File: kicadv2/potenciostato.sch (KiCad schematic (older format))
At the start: 33 parts, among them J10 test_GND, J11 test_GND, J12 test_GND, J13 AC2, J14 Conn_Coaxial, J3 Conn_01x03_Male, J4 test_I, J5 test_V, J6 test_VIN, J9 AC1, U1 OP77, U2 TL082, U3 OP77, U4 OP77, U5 4316, U6 L7805, U8 L7905

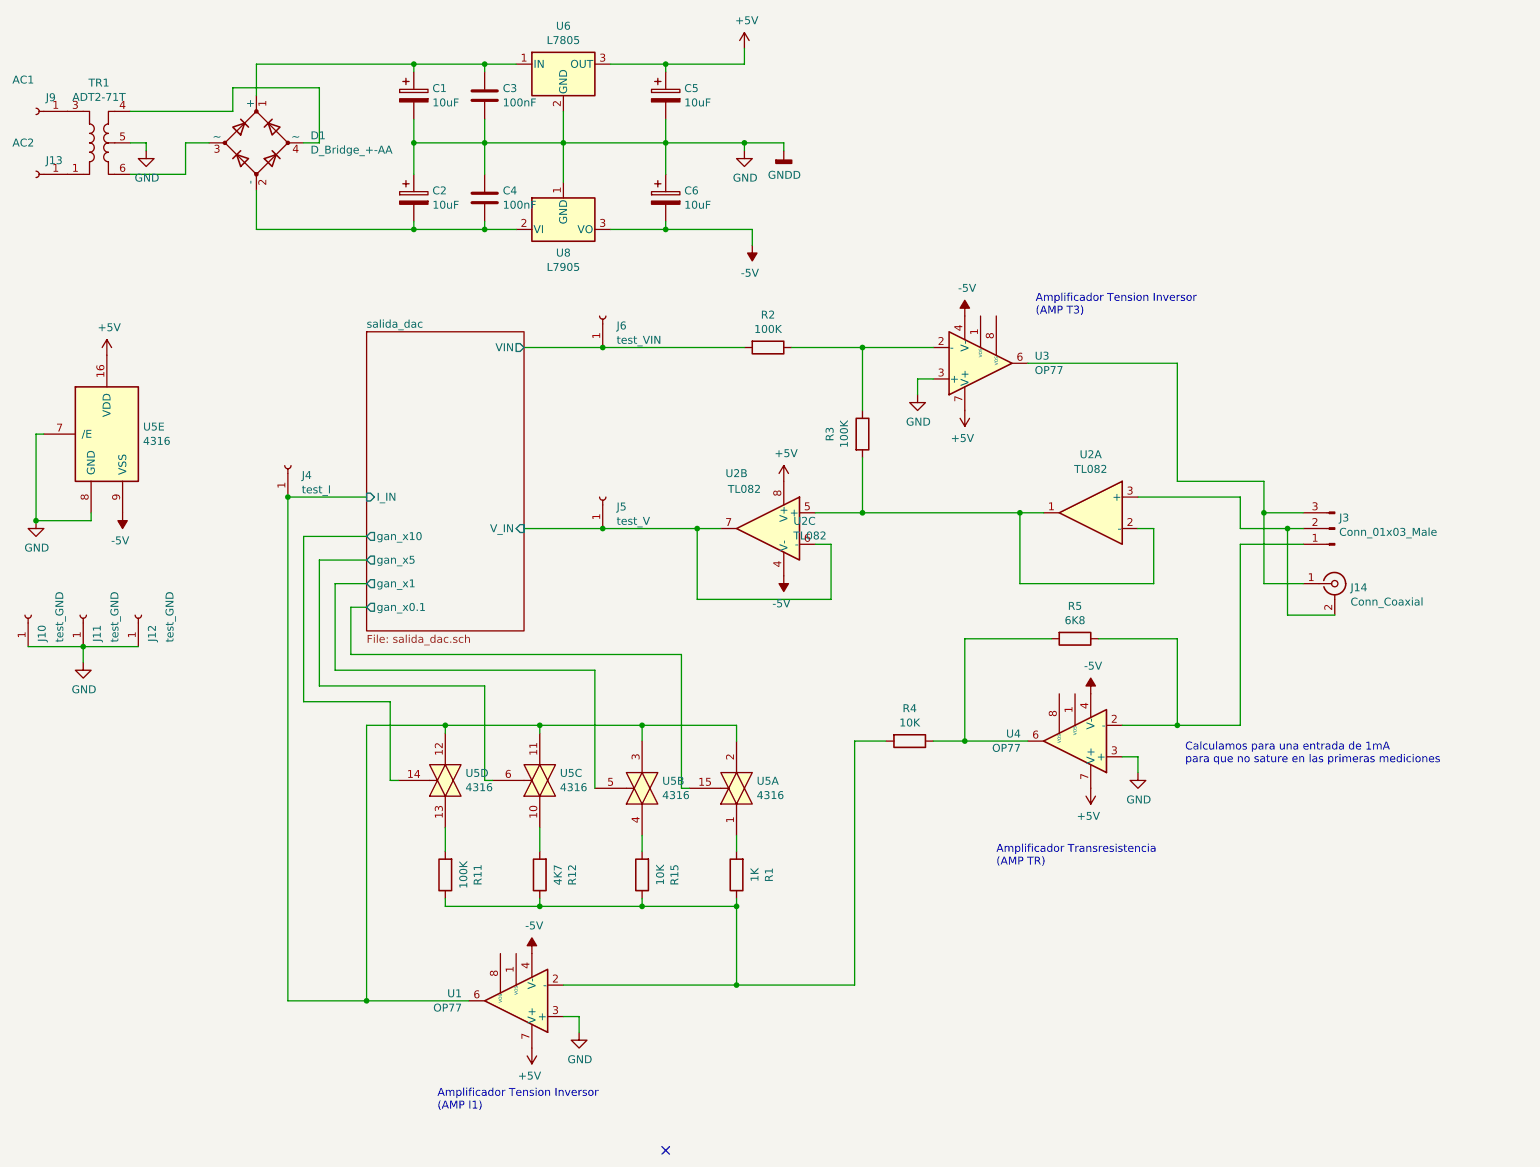
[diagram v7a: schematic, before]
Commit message: finalizado (casi) f silk, falta mover BNC para que no choqeu con LPC
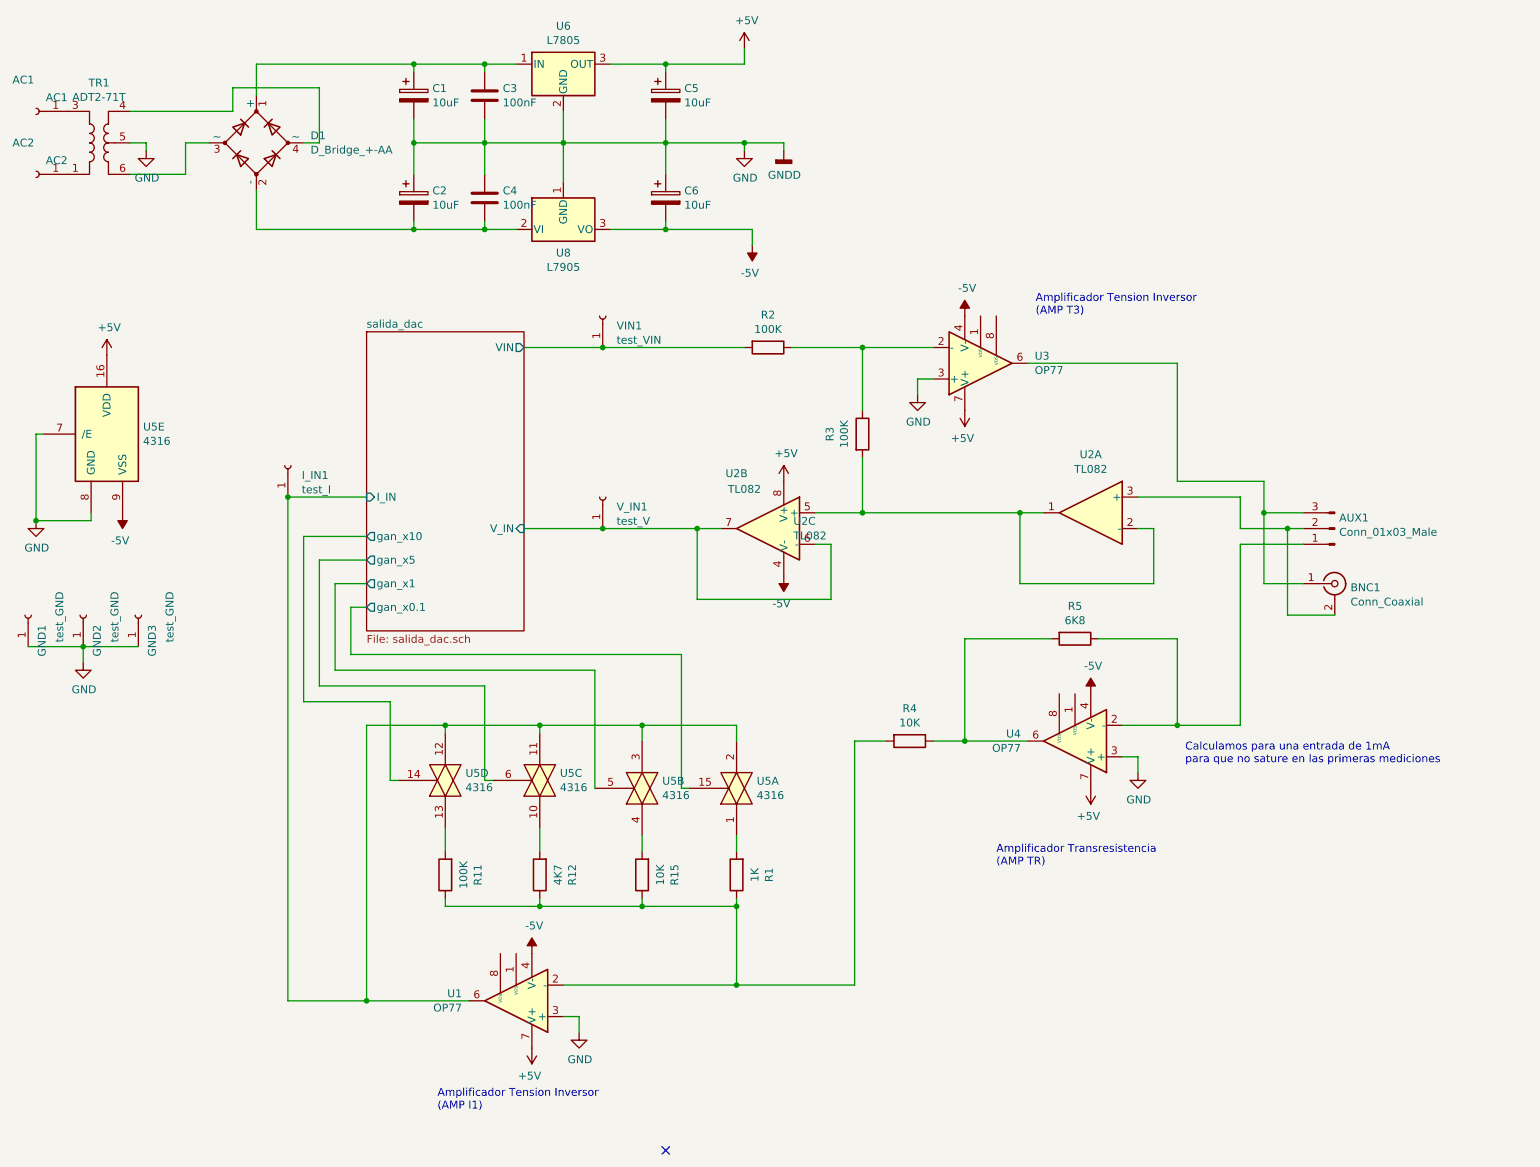
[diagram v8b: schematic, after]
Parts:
- renumbered J9 to AC1, J13 to AC2, J3 to AUX1, J14 to BNC1, J10 to GND1, J11 to GND2, J12 to GND3, J4 to I_IN1, J6 to VIN1, J5 to V_IN1
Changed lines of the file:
@@
 $EndComp
 $Comp
-L potenciostato-rescue:Conn_01x01_Female-Connector J4
+L potenciostato-rescue:Conn_01x01_Female-Connector I_IN1
 U 1 1 6185139C
 P 2550 3500
-F 0 "J4" V 2488 3412 50  0000 R CNN
+F 0 "I_IN1" V 2488 3412 50  0000 R CNN
 F 1 "test_I" V 2397 3412 50  0000 R CNN
 F 2 "Connector_PinHeader_2.54mm:PinHeader_1x01_P2.54mm_Vertical" H 2550 3500 50  0001 C CNN
@@
 $EndComp
 $Comp
-L potenciostato-rescue:Conn_01x01_Female-Connector J6
+L potenciostato-rescue:Conn_01x01_Female-Connector VIN1
 U 1 1 61851D11
 P 4550 2550
-F 0 "J6" V 4488 2462 50  0000 R CNN
+F 0 "VIN1" V 4488 2462 50  0000 R CNN
 F 1 "test_VIN" V 4397 2462 50  0000 R CNN
 F 2 "Connector_PinHeader_2.54mm:PinHeader_1x01_P2.54mm_Vertical" H 4550 2550 50  0001 C CNN
@@
 $EndComp
 $Comp
-L potenciostato-rescue:Conn_01x03_Male-Connector J3
+L potenciostato-rescue:Conn_01x03_Male-Connector AUX1
 U 1 1 5D250C0E
 P 9200 3900
-F 0 "J3" H 9172 3832 50  0000 R CNN
+F 0 "AUX1" H 9172 3832 50  0000 R CNN
 F 1 "Conn_01x03_Male" H 9172 3923 50  0000 R CNN
 F 2 "Connector_Phoenix_MC:PhoenixContact_MCV_1,5_3-G-3.5_1x03_P3.50mm_Vertical" H 9200 3900 50  0001 C CNN
@@
 	2550 3700 3050 3700
 $Comp
-L potenciostato-rescue:Conn_01x01_Female-Connector J5
+L potenciostato-rescue:Conn_01x01_Female-Connector V_IN1
 U 1 1 61851AC8
 P 4550 3700
-F 0 "J5" V 4488 3612 50  0000 R CNN
+F 0 "V_IN1" V 4488 3612 50  0000 R CNN
 F 1 "test_V" V 4397 3612 50  0000 R CNN
 F 2 "Connector_PinHeader_2.54mm:PinHeader_1x01_P2.54mm_Vertical" H 4550 3700 50  0001 C CNN
@@
 $EndComp
 $Comp
-L potenciostato-rescue:Conn_01x01_Female-Connector J12
+L potenciostato-rescue:Conn_01x01_Female-Connector GND3
 U 1 1 6185D9DF
 P 1600 4450
-F 0 "J12" H 1538 4362 50  0000 R CNN
+F 0 "GND3" H 1538 4362 50  0000 R CNN
 F 1 "test_GND" H 1750 4250 50  0000 R CNN
 F 2 "Connector_PinHeader_2.54mm:PinHeader_1x01_P2.54mm_Vertical" H 1600 4450 50  0001 C CNN
@@
 $EndComp
 $Comp
-L potenciostato-rescue:Conn_01x01_Female-Connector J11
+L potenciostato-rescue:Conn_01x01_Female-Connector GND2
 U 1 1 6185DEE6
 P 1250 4450
-F 0 "J11" H 1188 4362 50  0000 R CNN
+F 0 "GND2" H 1188 4362 50  0000 R CNN
 F 1 "test_GND" H 1400 4250 50  0000 R CNN
 F 2 "Connector_PinHeader_2.54mm:PinHeader_1x01_P2.54mm_Vertical" H 1250 4450 50  0001 C CNN
@@
 $EndComp
 $Comp
-L potenciostato-rescue:Conn_01x01_Female-Connector J10
+L potenciostato-rescue:Conn_01x01_Female-Connector GND1
 U 1 1 6185E017
 P 900 4450
-F 0 "J10" H 838 4362 50  0000 R CNN
+F 0 "GND1" H 838 4362 50  0000 R CNN
 F 1 "test_GND" H 1050 4250 50  0000 R CNN
 F 2 "Connector_PinHeader_2.54mm:PinHeader_1x01_P2.54mm_Vertical" H 900 4450 50  0001 C CNN
@@
 	4550 2750 5450 2750
 $Comp
-L potenciostato-rescue:Conn_01x01_Female-Connector J13
+L potenciostato-rescue:Conn_01x01_Female-Connector AC2
 U 1 1 63685931
 P 950 1650
-F 0 "J13" H 888 1562 50  0000 R CNN
+F 0 "AC2" H 888 1562 50  0000 R CNN
 F 1 "AC2" H 1100 1450 50  0000 R CNN
 F 2 "Connector_PinHeader_2.54mm:PinHeader_1x01_P2.54mm_Vertical" H 950 1650 50  0001 C CNN
@@
 $EndComp
 $Comp
-L potenciostato-rescue:Conn_01x01_Female-Connector J9
+L potenciostato-rescue:Conn_01x01_Female-Connector AC1
 U 1 1 636995B8
 P 950 1250
-F 0 "J9" H 888 1162 50  0000 R CNN
+F 0 "AC1" H 888 1162 50  0000 R CNN
 F 1 "AC1" H 1100 1050 50  0000 R CNN
 F 2 "Connector_PinHeader_2.54mm:PinHeader_1x01_P2.54mm_Vertical" H 950 1250 50  0001 C CNN
@@
 Connection ~ 5450 1450
 $Comp
-L Connector:Conn_Coaxial J14
+L Connector:Conn_Coaxial BNC1
 U 1 1 636ED754
 P 9200 4250
-F 0 "J14" H 9300 4225 50  0000 L CNN
+F 0 "BNC1" H 9300 4225 50  0000 L CNN
 F 1 "Conn_Coaxial" H 9300 4134 50  0000 L CNN
 F 2 "Connector_Coaxial:BNC_Amphenol_B6252HB-NPP3G-50_Horizontal" H 9200 4250 50  0001 C CNN
